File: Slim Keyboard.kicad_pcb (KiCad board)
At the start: 2 copper layers, 67 x 74 mm, 61 parts, among them J1 USB_C_Receptacle_USB2.0_16P, J2 SWD, J3 SWC, J4 Conn_01x14_Pin, J5 JST to Battery, J6 Conn_01x14_Pin, U1 NRF52840-QIAA-R, U2 BQ24075RGT, U3 XC6220B331MR, Y1 FC-12M 32.7680KA-AC0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

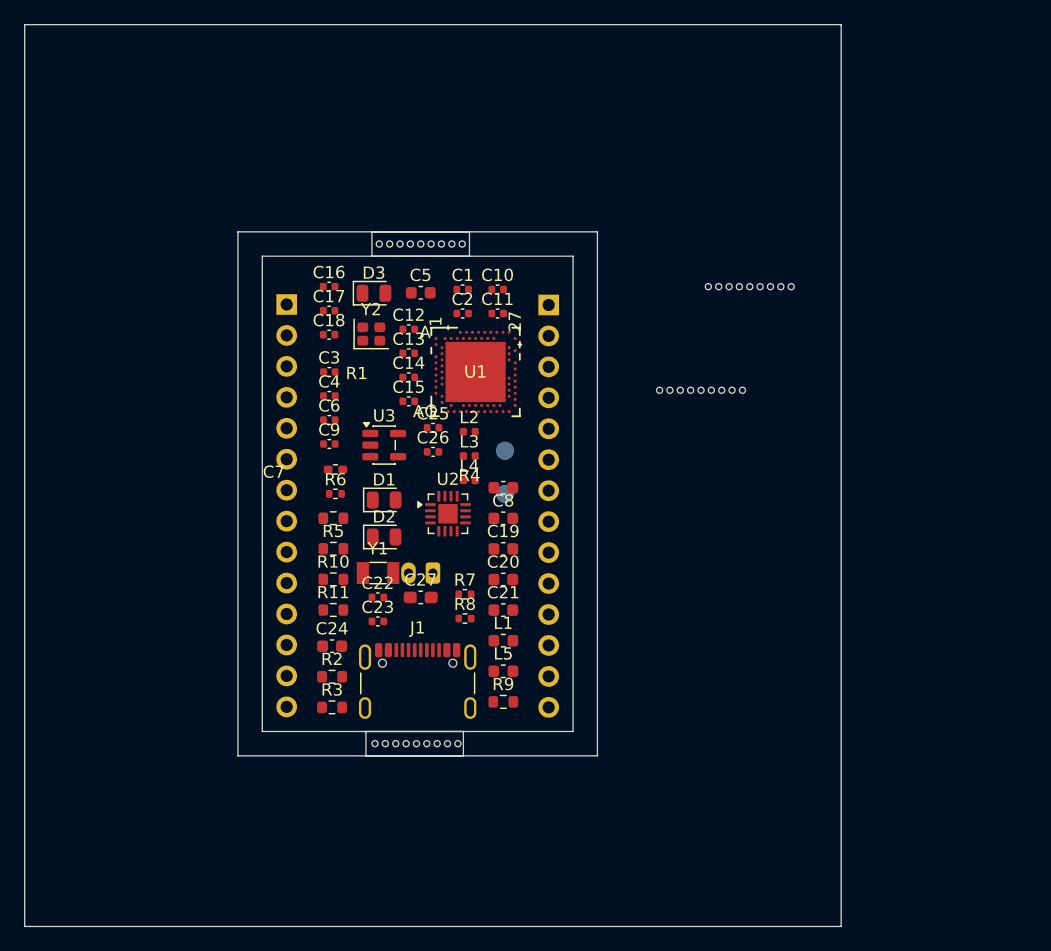
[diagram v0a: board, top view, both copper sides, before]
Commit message: Adjusted PCB Test Layout
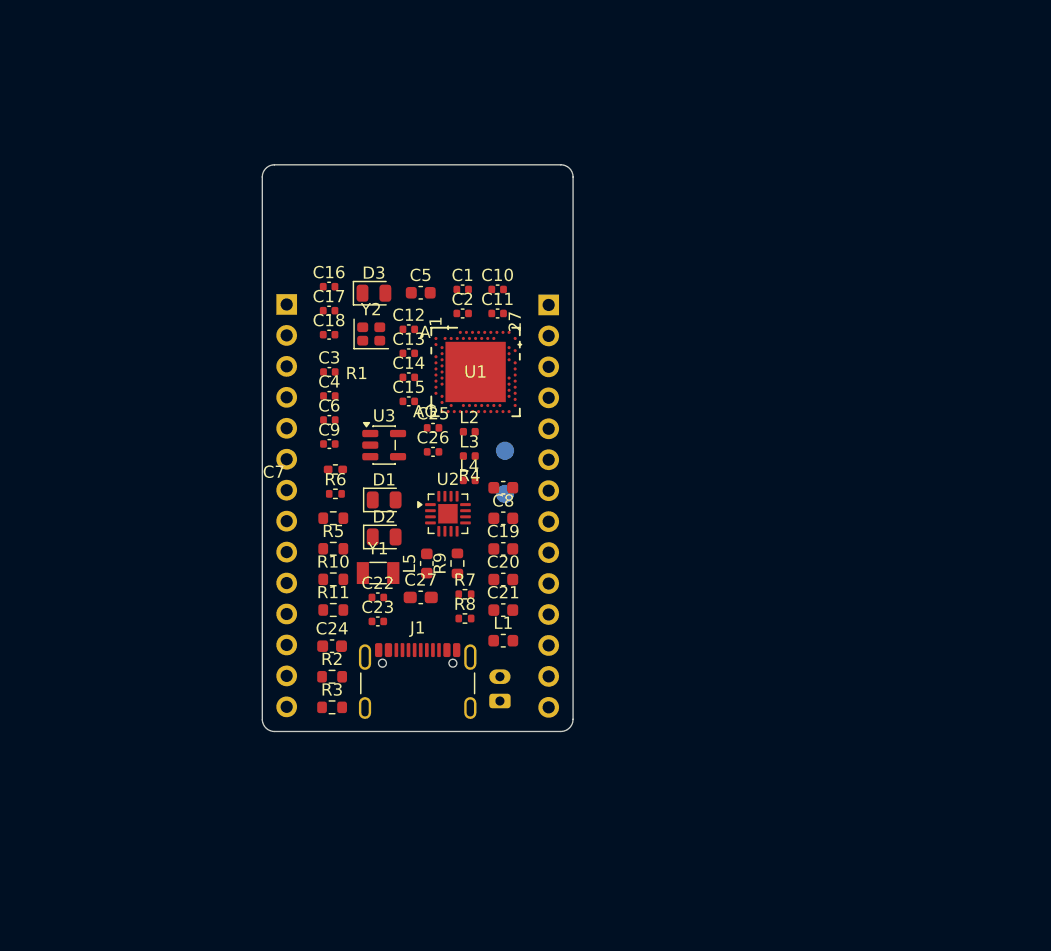
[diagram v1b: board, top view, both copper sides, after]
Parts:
- removed rBT1, rBT2, rBT3, rBT4: Breakaway Tabs, Panelization:BreakLine_9h_D0.5mm_P0.85mm
- moved R9 12.0 mm to (49.5, 70.2), turned to 90 degrees
- moved J5 11.9 mm to (53.0, 81.5), turned to 90 degrees
- moved L5 10.8 mm to (47.0, 70.2), turned to 90 degrees
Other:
- board size 67 x 74 mm -> 25.5 x 46.5 mm

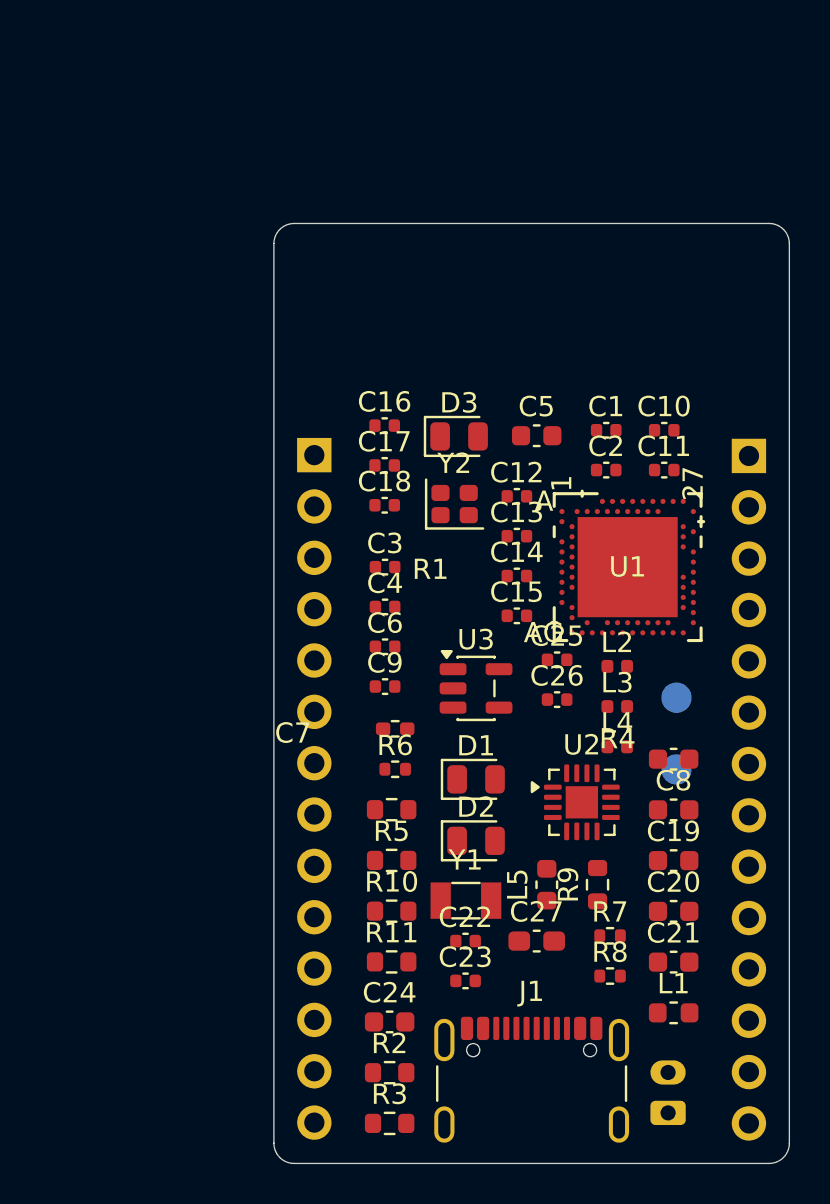
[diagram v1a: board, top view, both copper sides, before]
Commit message: Added actual JST connector
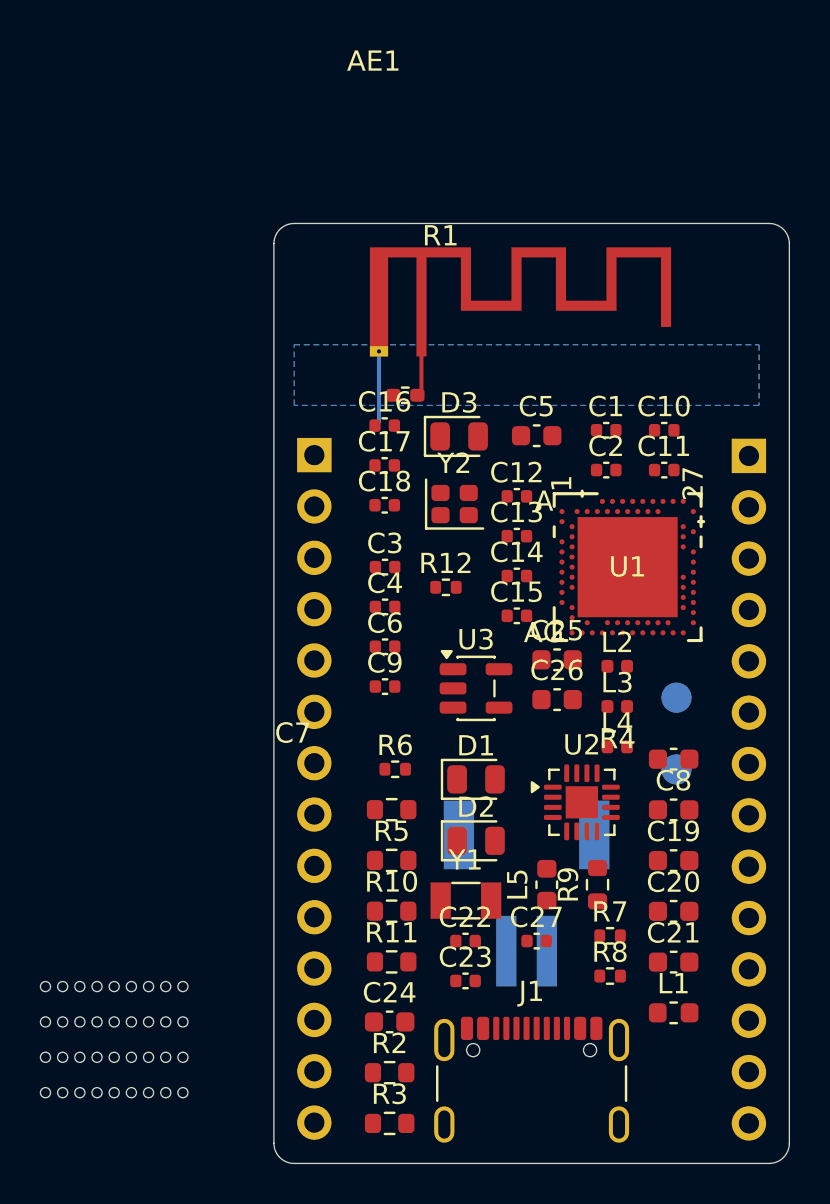
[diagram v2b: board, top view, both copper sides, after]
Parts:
- added AE1: Antenna_Shield, Antenna:2.4GHz F Antenna, F.Cu at (38.2, 38.7)
- added R12: 1M, Resistor_SMD:R_0402_1005Metric, F.Cu at (42.0, 55.5)
- added rBT1: Breakaway Tabs, Panelization:BreakLine_9h_D0.5mm_P0.85mm, F.Cu at (25.6, 75.2)
- added rBT2: Breakaway Tabs, Panelization:BreakLine_9h_D0.5mm_P0.85mm, F.Cu at (25.6, 77.0)
- added rBT3: Breakaway Tabs, Panelization:BreakLine_9h_D0.5mm_P0.85mm, F.Cu at (25.6, 78.8)
- added rBT4: Breakaway Tabs, Panelization:BreakLine_9h_D0.5mm_P0.85mm, F.Cu at (25.6, 80.5)
- C25, C26: footprint Capacitor_SMD:C_0402_1005Metric -> Capacitor_SMD:C_0603_1608Metric
- C27: value 1nF -> 4.7nF; footprint Capacitor_SMD:C_0603_1608Metric_Pad1.08x0.95mm_HandSolder -> Capacitor_SMD:C_0402_1005Metric
- J5: value JST to Battery -> S2B-PH-SM4-TB; footprint Connector_JST:JST_PH_S2B-PH-K_1x02_P2.00mm_Horizontal -> S2B-PH-SM4-TB:JST_S2B-PH-SM4-TB
- moved R1 16.5 mm to (40.0, 46.0)
- moved J5 10.6 mm to (46.0, 73.5), turned to 180 degrees
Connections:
- R1 pad 2: ANTENNA -> Net-(AE1-A)
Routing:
- net Net-(AE1-A): track 0.00 -> 4.45 mm
- net GND: track 0.00 -> 3.75 mm
- added copper zone on B.Cu, net GND

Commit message: Adjusted Footprint sizes
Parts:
- C23: footprint Capacitor_SMD:C_0402_1005Metric -> Capacitor_SMD:C_0603_1608Metric
- R10: value N.C. -> 3.1k; footprint Resistor_SMD:R_0603_1608Metric -> Resistor_SMD:R_0402_1005Metric
- R11, R2, R3, R4, R5: footprint Resistor_SMD:R_0603_1608Metric -> Resistor_SMD:R_0402_1005Metric
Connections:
- R4 pad 2: VBUS -> VDDH
- R5 pad 2: VBUS -> VDDH

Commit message: Started PCB design
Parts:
- removed J4, J6: Conn_01x14_Pin, Connector_PinHeader_2.54mm:PinHeader_1x14_P2.54mm_Vertical
- removed rBT1, rBT2, rBT3, rBT4: Breakaway Tabs, Panelization:BreakLine_9h_D0.5mm_P0.85mm
- added J7: ~, KBSlim_NRF52840_module:NRF52840_module, F.Cu at (70.0, 40.2)
- C16: value 1pF -> 1.2pF
- D1: value Orange -> LTST-C170KFKT
- D2: value Green -> LTST-C170KGKT
- D3: value BLUE -> IN-S85AT5B
- R4, R5, R9: value R -> 1k
- Y1: value FC-12M 32.7680KA-AC0 -> ECS-.327-9-34B-TR
- moved AE1 68.8 mm to (91.0, 83.0), turned to 180 degrees
- moved R5 54.6 mm to (91.0, 51.2), turned to 180 degrees
- moved R4 53.5 mm to (91.0, 52.5), turned to 180 degrees
- moved J1 53.0 mm to (83.0, 42.9), turned to 180 degrees
- moved R3 51.9 mm to (61.1, 34.9)
- moved R2 51.5 mm to (61.1, 32.9)
- moved D2 51.3 mm to (90.2, 47.0)
- moved D1 50.9 mm to (90.2, 44.8)
- moved Y2 49.5 mm to (89.3, 67.3)
- moved D3 47.6 mm to (90.2, 49.2)
- moved Y1 45.5 mm to (86.8, 58.4)
- moved C22 45.3 mm to (64.0, 32.9)
- moved J5 45.1 mm to (83.0, 47.6), turned to 0 degrees
- moved U2 40.2 mm to (86.8, 53.1), turned to 90 degrees
- moved R11 38.0 mm to (61.1, 42.9)
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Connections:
- U1 pad AD10: unconnected-(U1-P0.15-PadAD10) -> BLED
- U1 pad AD8: unconnected-(U1-P0.13-PadAD8) -> POWER_PIN
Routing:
- net GND: track 3.75 -> 18.3 mm
- net VDDH: track 0.00 -> 13.9 mm
- net POWER_PIN: track 0.00 -> 13.4 mm
- net Net-(D1-A): track 0.00 -> 8.60 mm
- net Net-(D1-K): track 0.00 -> 7.63 mm
- net Net-(D2-K): track 0.00 -> 6.88 mm
- net Net-(D2-A): track 0.00 -> 4.77 mm
- net Net-(AE1-A): track 4.45 -> 0.00 mm
- added copper zone on F.Cu, net GND
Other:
- board size 25.5 x 46.5 mm -> 26 x 45.5 mm

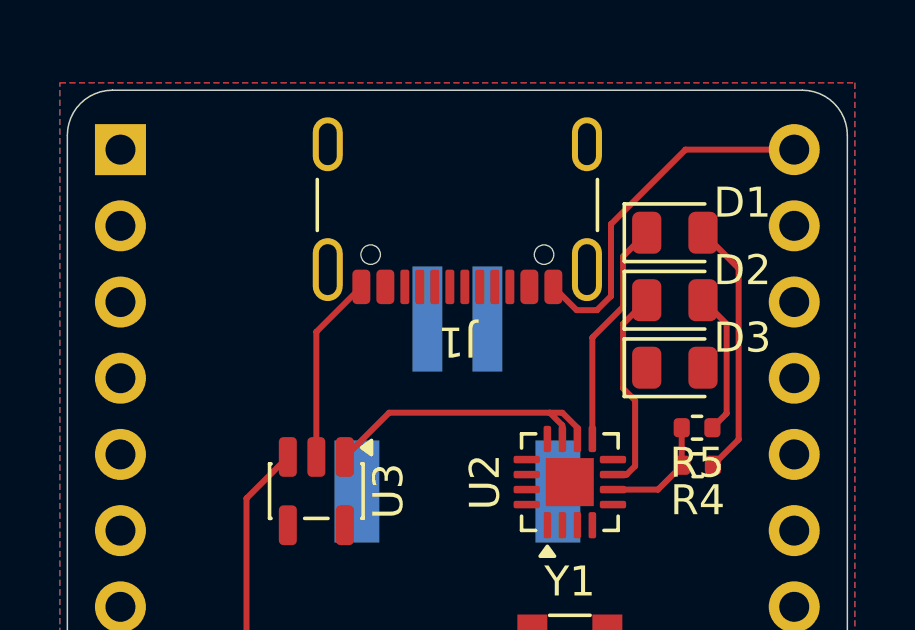
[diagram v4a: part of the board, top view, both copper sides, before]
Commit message: Connected GPIO
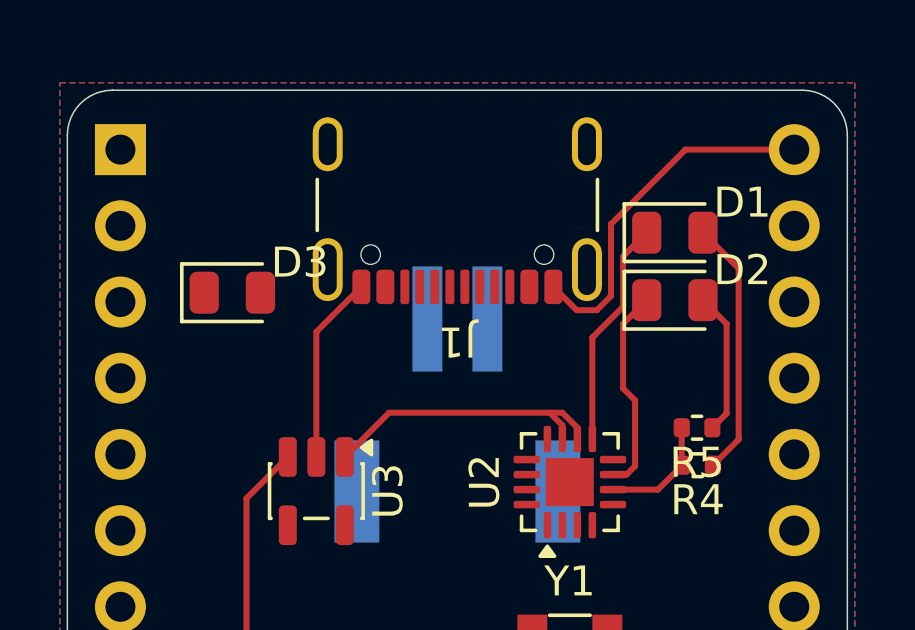
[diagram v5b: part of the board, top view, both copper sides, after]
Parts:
- moved D3 15.0 mm to (75.5, 46.8)
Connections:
- J7 pad 10: unconnected-(J7-Pad10) -> PH5
- J7 pad 11: unconnected-(J7-Pad11) -> PH6
- J7 pad 12: unconnected-(J7-Pad12) -> PH7
- J7 pad 13: unconnected-(J7-Pad13) -> PH8
- J7 pad 14: unconnected-(J7-Pad14) -> PH9
- J7 pad 15: unconnected-(J7-Pad15) -> PL10
- J7 pad 16: unconnected-(J7-Pad16) -> PL11
- J7 pad 17: unconnected-(J7-Pad17) -> PL12
- J7 pad 18: unconnected-(J7-Pad18) -> PL13
- J7 pad 19: unconnected-(J7-Pad19) -> PL14
- J7 pad 2: unconnected-(J7-Pad2) -> EXT_VCC
- J7 pad 20: unconnected-(J7-Pad20) -> PL15
- J7 pad 21: unconnected-(J7-Pad21) -> PL16
- J7 pad 22: unconnected-(J7-Pad22) -> PL17
- J7 pad 23: unconnected-(J7-Pad23) -> PL18
- J7 pad 24: unconnected-(J7-Pad24) -> PL19
- J7 pad 25: unconnected-(J7-Pad25) -> GND
- J7 pad 26: unconnected-(J7-Pad26) -> SYSOFF_SWITCH
- J7 pad 27: unconnected-(J7-Pad27) -> VDDH
- J7 pad 3: unconnected-(J7-Pad3) -> RESET
- J7 pad 4: unconnected-(J7-Pad4) -> GND
- J7 pad 5: unconnected-(J7-Pad5) -> PH0
- J7 pad 6: unconnected-(J7-Pad6) -> PH1
- J7 pad 7: unconnected-(J7-Pad7) -> PH2
- J7 pad 8: unconnected-(J7-Pad8) -> PH3
- J7 pad 9: unconnected-(J7-Pad9) -> PH4
- U1 pad A10: unconnected-(U1-P0.29/AIN5-PadA10) -> PL17
- U1 pad A12: unconnected-(U1-P0.02/AIN0-PadA12) -> PL15
- U1 pad A14: unconnected-(U1-P1.15-PadA14) -> PL13
- U1 pad A16: unconnected-(U1-P1.13-PadA16) -> PL11
- U1 pad A8: unconnected-(U1-P0.31/AIN7-PadA8) -> PL19
- U1 pad AC11: unconnected-(U1-P0.16-PadAC11) -> PH0
- U1 pad AC15: unconnected-(U1-P0.19-PadAC15) -> PH2
- U1 pad AC17: unconnected-(U1-P0.21-PadAC17) -> PH4
- U1 pad AC19: unconnected-(U1-P0.23-PadAC19) -> PH6
- U1 pad AC21: unconnected-(U1-P0.25-PadAC21) -> PH8
- U1 pad AD12: unconnected-(U1-P0.17-PadAD12) -> PH1
- U1 pad AD16: unconnected-(U1-P0.20-PadAD16) -> PH3
- U1 pad AD18: unconnected-(U1-P0.22-PadAD18) -> PH5
- U1 pad AD20: unconnected-(U1-P0.24-PadAD20) -> PH7
- U1 pad AD22: unconnected-(U1-P1.00-PadAD22) -> PH9
- U1 pad B11: unconnected-(U1-P0.28/AIN4-PadB11) -> PL16
- U1 pad B13: unconnected-(U1-P0.03/AIN1-PadB13) -> PL14
- U1 pad B15: unconnected-(U1-P1.14-PadB15) -> PL12
- U1 pad B17: unconnected-(U1-P1.12-PadB17) -> PL10
- U1 pad B9: unconnected-(U1-P0.30/AIN6-PadB9) -> PL18

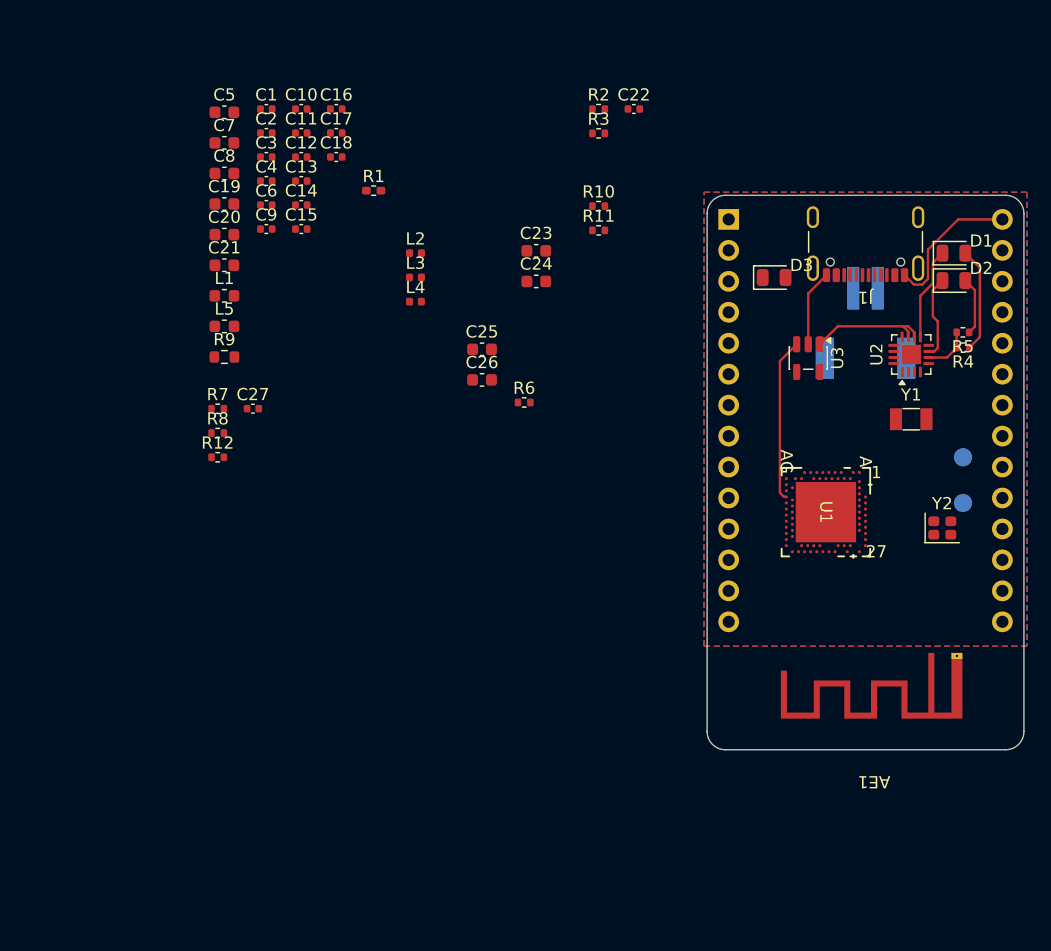
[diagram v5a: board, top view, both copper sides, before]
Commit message: Placed Components and started routing
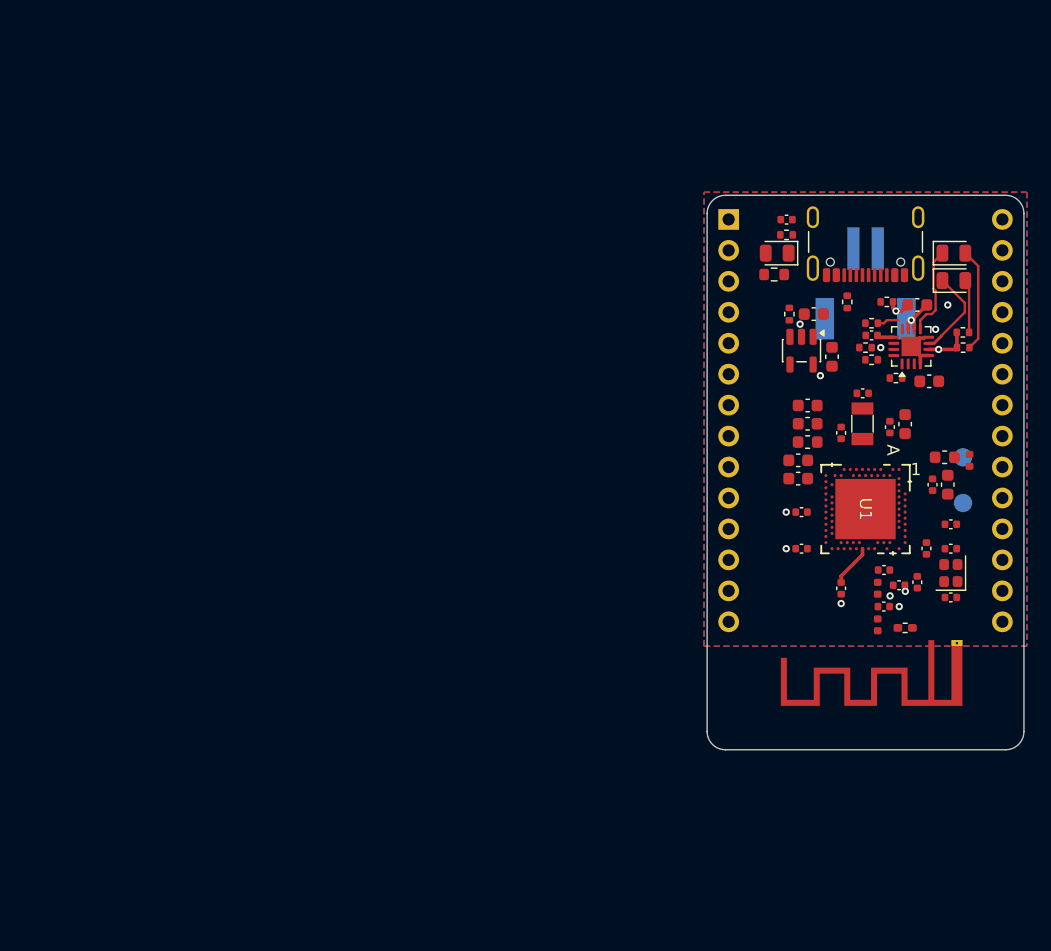
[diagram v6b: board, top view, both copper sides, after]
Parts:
- moved C8 64.6 mm to (89.8, 63.8), turned to 90 degrees
- moved C12 64.4 mm to (90.0, 73.0), turned to 180 degrees
- moved C11 63.3 mm to (90.0, 69.0)
- moved C10 63.3 mm to (90.0, 67.0)
- moved C6 61.1 mm to (88.0, 69.0), turned to 90 degrees
- moved C16 60.7 mm to (84.5, 73.8), turned to 180 degrees
- moved L1 60.6 mm to (89.5, 61.5)
- moved C7 60.4 mm to (86.2, 58.8), turned to -90 degrees
- moved C13 60.3 mm to (87.2, 71.8), turned to 90 degrees
- moved C9 58.6 mm to (88.5, 63.8), turned to 90 degrees
- moved C14 58.1 mm to (85.8, 72.0)
- moved C1 56.8 mm to (77.8, 69.0), turned to 180 degrees
- moved C2 56.6 mm to (85.0, 59.0), turned to 90 degrees
- moved R1 56.5 mm to (86.2, 75.5)
- moved C17 55.8 mm to (81.0, 72.2), turned to -90 degrees
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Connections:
- Y2 pad 1: GND -> Net-(U1-XC1)
- Y2 pad 2: Net-(U1-XC2) -> GND
- Y2 pad 3: GND -> Net-(U1-XC2)
- Y2 pad 4: Net-(U1-XC1) -> GND
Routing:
- net POWER_PIN: track 13.4 -> 0.07 mm
- net GND: track 18.3 -> 6.03 mm, vias 0 -> 7
- net VDDH: track 13.9 -> 7.59 mm, vias 0 -> 2
- net Net-(U1-DEC5): track 0.00 -> 3.49 mm
- net Net-(U2-ILIM): track 0.00 -> 1.84 mm
- net VBUS: track 0.00 -> 1.39 mm
- net Net-(D2-K): track 6.88 -> 7.39 mm
- net EXT_VCC: track 0.00 -> 0.50 mm, vias 0 -> 1
- net SYSOFF_SWITCH: vias 0 -> 1
- net Net-(U1-DEC4): vias 0 -> 1
- net (no net): vias 0 -> 2
